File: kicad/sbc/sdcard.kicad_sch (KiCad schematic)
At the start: 12 parts, among them U14 7407, U15 SD_Card, U7 74125, U9 LP2950

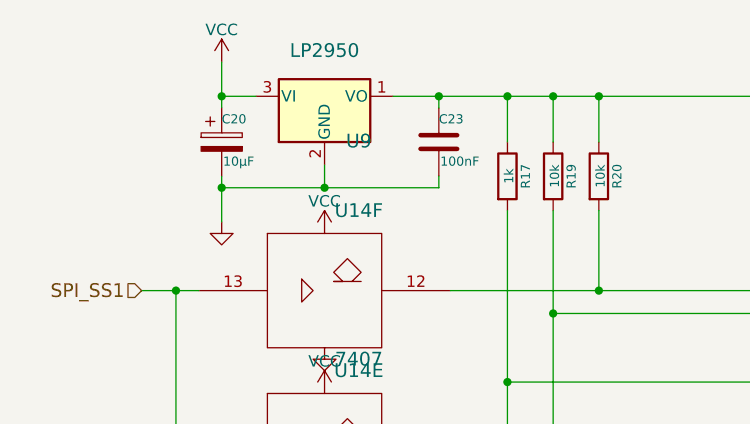
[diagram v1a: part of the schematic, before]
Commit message: cpld pinout
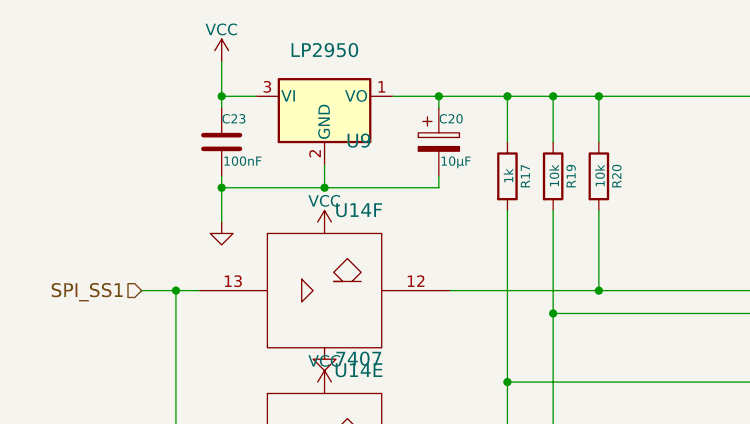
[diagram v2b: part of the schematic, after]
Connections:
- net VCC: now also C23.1; no longer C20.1
- net at C24.1, R17.1, R19.1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: now also C20.1; no longer C23.1
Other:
- moved on the sheet: C20, C23
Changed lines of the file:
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@@
     )
   )
-  (symbol (lib_id "Device:C_Polarized") (at 54.61 43.18 0) (unit 1)
-    (in_bom yes) (on_board yes) (dnp no)
-    (property "Reference" "C20" (at 54.61 40.64 0)
-      (effects (font (size 1.016 1.016)) (justify left))
-    )
-    (property "Value" "10µF" (at 54.7624 45.339 0)
-      (effects (font (size 1.016 1.016)) (justify left))
-    )
-    (property "Footprint" "Capacitor_THT:CP_Radial_D5.0mm_P2.50mm" (at 55.5752 46.99 0)
-      (effects (font (size 1.27 1.27)) hide)
-    )
-    (property "Datasheet" "~" (at 54.61 43.18 0)
+  (symbol (lib_id "Device:C_Polarized") (at 78.74 43.18 0) (unit 1)
+    (in_bom yes) (on_board yes) (dnp no)
+    (property "Reference" "C20" (at 78.74 40.64 0)
+      (effects (font (size 1.016 1.016)) (justify left))
+    )
+    (property "Value" "10µF" (at 78.8924 45.339 0)
+      (effects (font (size 1.016 1.016)) (justify left))
+    )
+    (property "Footprint" "Capacitor_THT:CP_Radial_D5.0mm_P2.50mm" (at 79.7052 46.99 0)
+      (effects (font (size 1.27 1.27)) hide)
+    )
+    (property "Datasheet" "~" (at 78.74 43.18 0)
       (effects (font (size 1.27 1.27)) hide)
     )
@@
     )
   )
-  (symbol (lib_id "Device:C") (at 78.74 43.18 0) (unit 1)
-    (in_bom yes) (on_board yes) (dnp no)
-    (property "Reference" "C23" (at 78.74 40.64 0)
-      (effects (font (size 1.016 1.016)) (justify left))
-    )
-    (property "Value" "100nF" (at 78.8924 45.339 0)
-      (effects (font (size 1.016 1.016)) (justify left))
-    )
-    (property "Footprint" "Capacitor_SMD:C_1206_3216Metric_Pad1.33x1.80mm_HandSolder" (at 79.7052 46.99 0)
-      (effects (font (size 1.27 1.27)) hide)
-    )
-    (property "Datasheet" "~" (at 78.74 43.18 0)
-      (effects (font (size 1.27 1.27)) hide)
-    )
+  (symbol (lib_id "Device:C") (at 54.61 43.18 0) (unit 1)
+    (in_bom yes) (on_board yes) (dnp no)
+    (property "Reference" "C23" (at 54.61 40.64 0)
+      (effects (font (size 1.016 1.016)) (justify left))
+    )
+    (property "Value" "100nF" (at 54.7624 45.339 0)
+      (effects (font (size 1.016 1.016)) (justify left))
+    )
+    (property "Footprint" "Capacitor_SMD:C_1206_3216Metric_Pad1.33x1.80mm_HandSolder" (at 55.5752 46.99 0)
+      (effects (font (size 1.27 1.27)) hide)
+    )
+    (property "Datasheet" "~" (at 54.61 43.18 0)
+      (effects (font (size 1.27 1.27)) hide)
+    )

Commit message: complete schematics
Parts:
- removed U15: SD_Card, Connector_Card:SD_TE_2041021, symbol Connector:SD_Card
- added U15: Micro_SD_Card_Det1, Connector_Card:microSD_HC_Hirose_DM3BT-DSF-PEJS, symbol Connector:Micro_SD_Card_Det1
- U14, U7: footprint Package_DIP:DIP-14_W7.62mm_Socket_LongPads -> Package_DIP:DIP-14_W7.62mm_LongPads
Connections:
- net GND: now also U15.10 (SHIELD), U15.4 (VDD)
- net SD_CARD_DETECT: now also U15.9 (DET)
- net at C20.1, C24.1, R17.1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: now also U15.6 (VSS)
- net DAT3: now reaches R20.2, U14.12
- net DAT3: now also U15.2 (DAT3/CD)
- net CMD: now reaches R19.2, U14.10
- net CMD: now also U15.3 (CMD)
- net CLK: now reaches R17.2, U14.8
- net CLK: now also U15.5 (CLK)
- net DAT0: now reaches U7.9 (D)
- net DAT0: now also U15.7 (DAT0)
- net DAT1: now reaches R21.2
- net DAT1: now also U15.8 (DAT1)
- net DAT2: now reaches R22.2
- net DAT2: now also U15.1 (DAT2)
- no-connect marks 2 -> 0

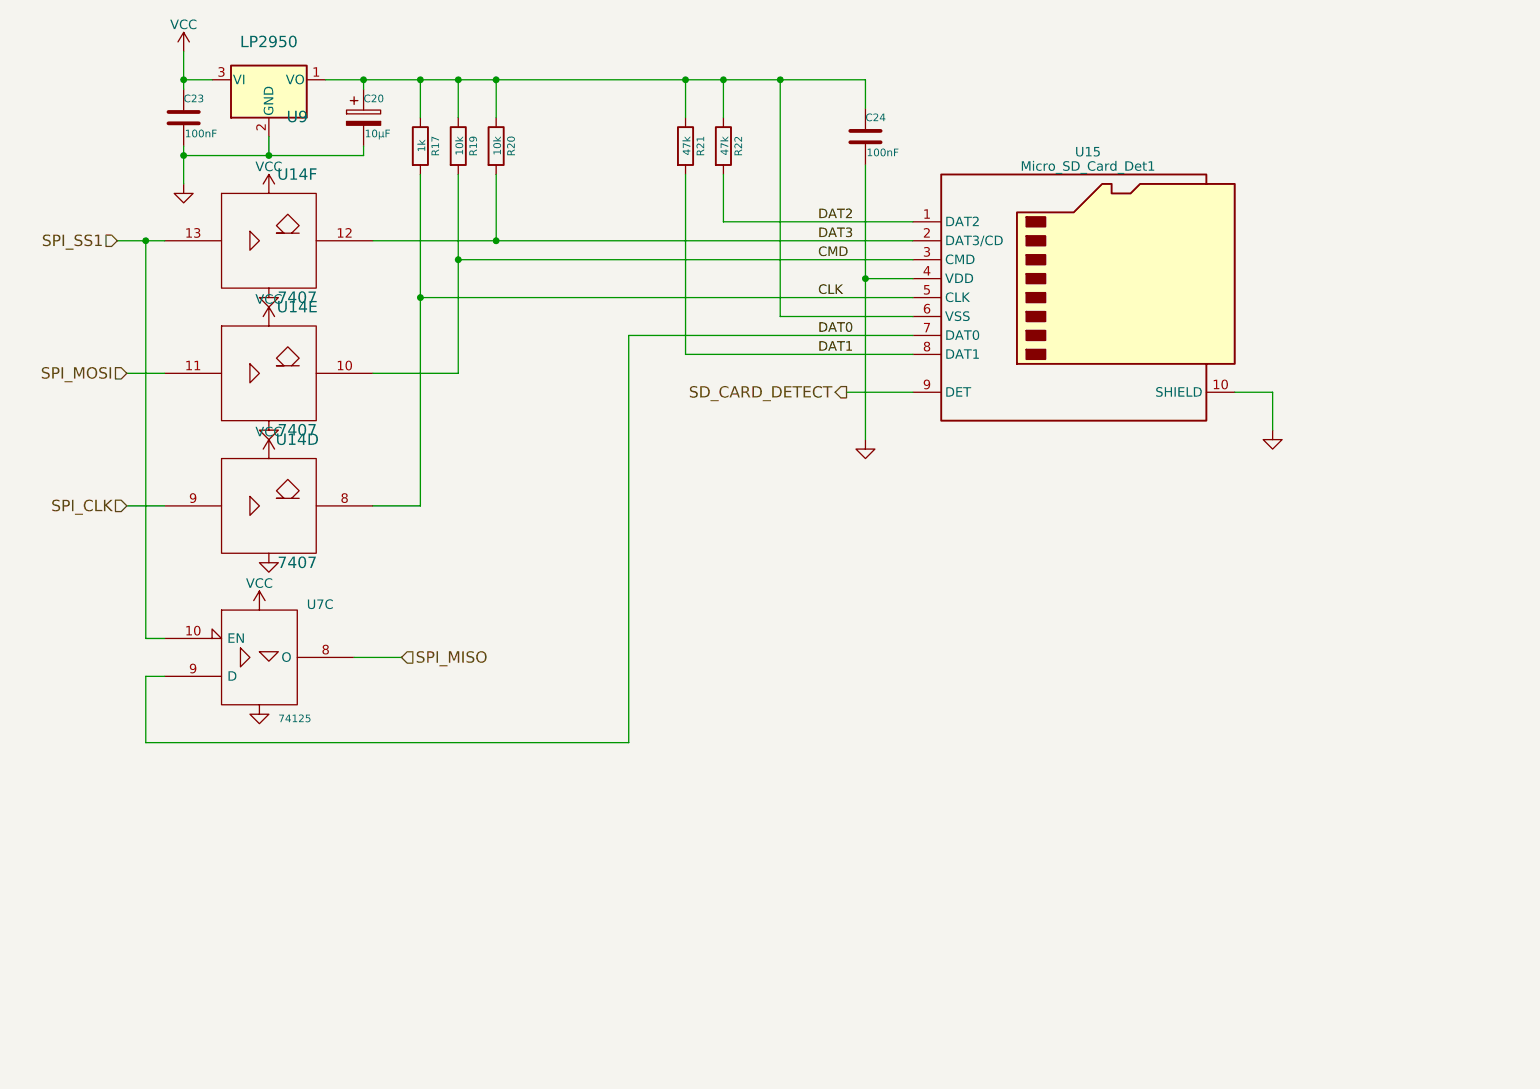
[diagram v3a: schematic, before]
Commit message: fix ERC messages
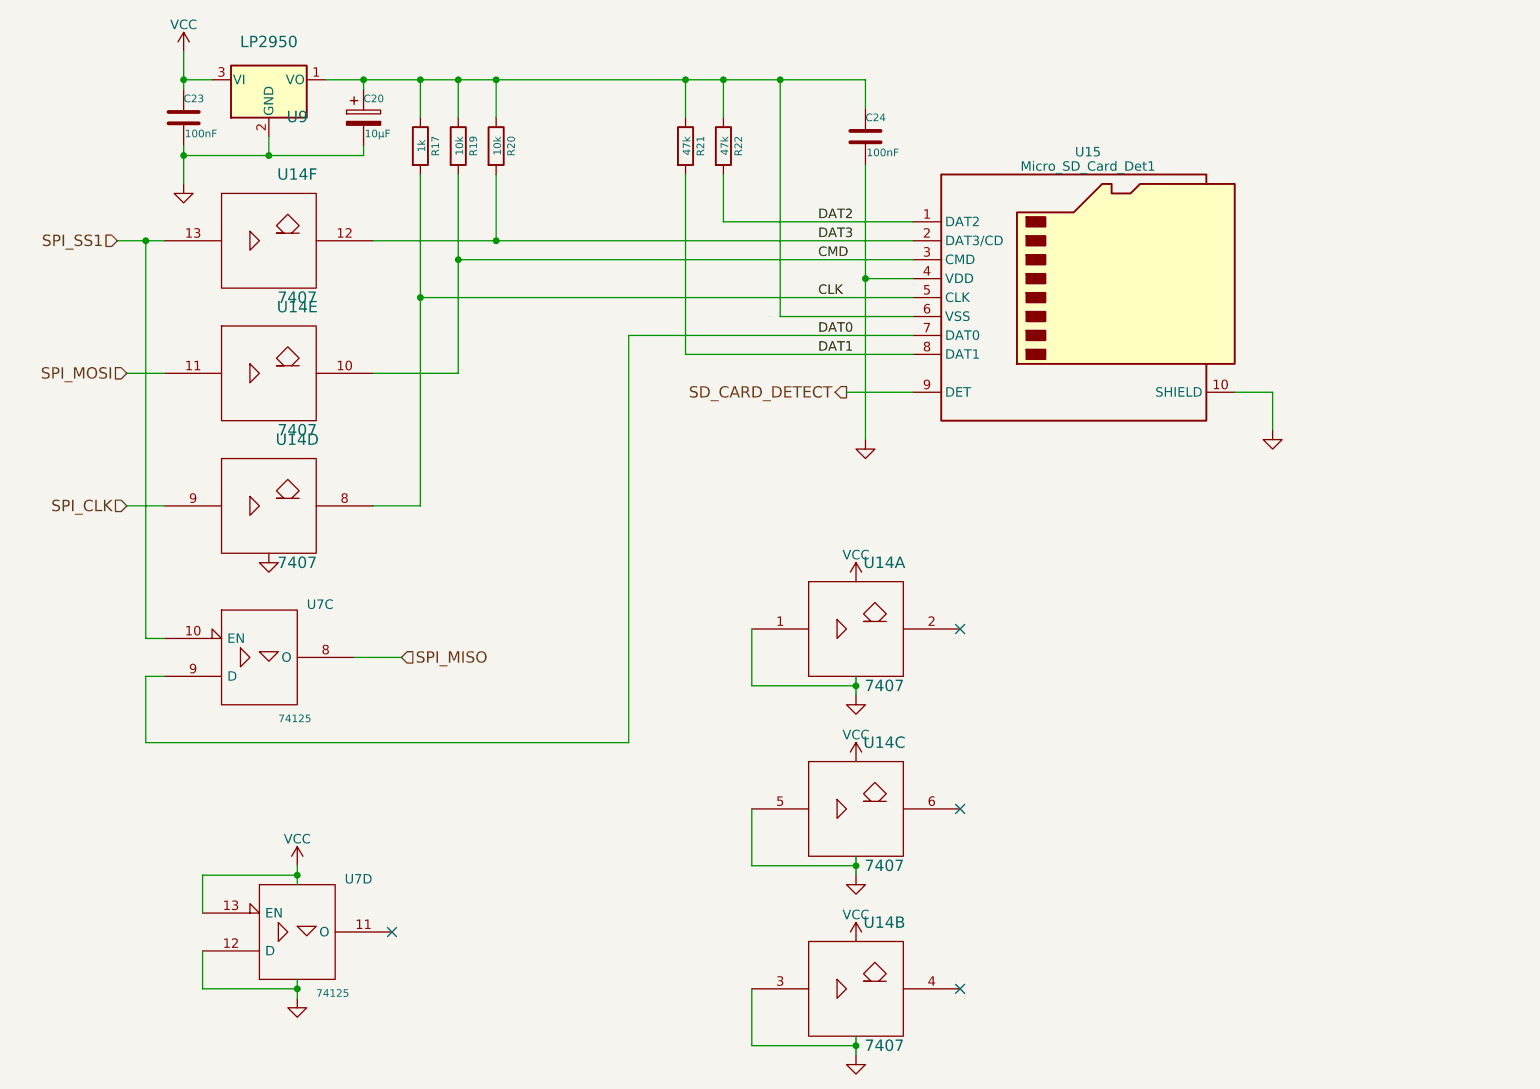
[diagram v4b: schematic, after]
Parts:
- added unit 1 of U14
- added unit 3 of U14
- added unit 2 of U14
- added unit 4 of U7
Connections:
- net GND: now also U14.1, U14.3, U14.5, U14.7 (Gnd), U14.7 (Gnd), U14.7 (Gnd), U7.12 (D), U7.7 (GND)
- net VCC: now also U14.14 (Vcc), U14.14 (Vcc), U14.14 (Vcc), U7.13 (EN), U7.14 (VCC)
- no-connect marks 0 -> 4

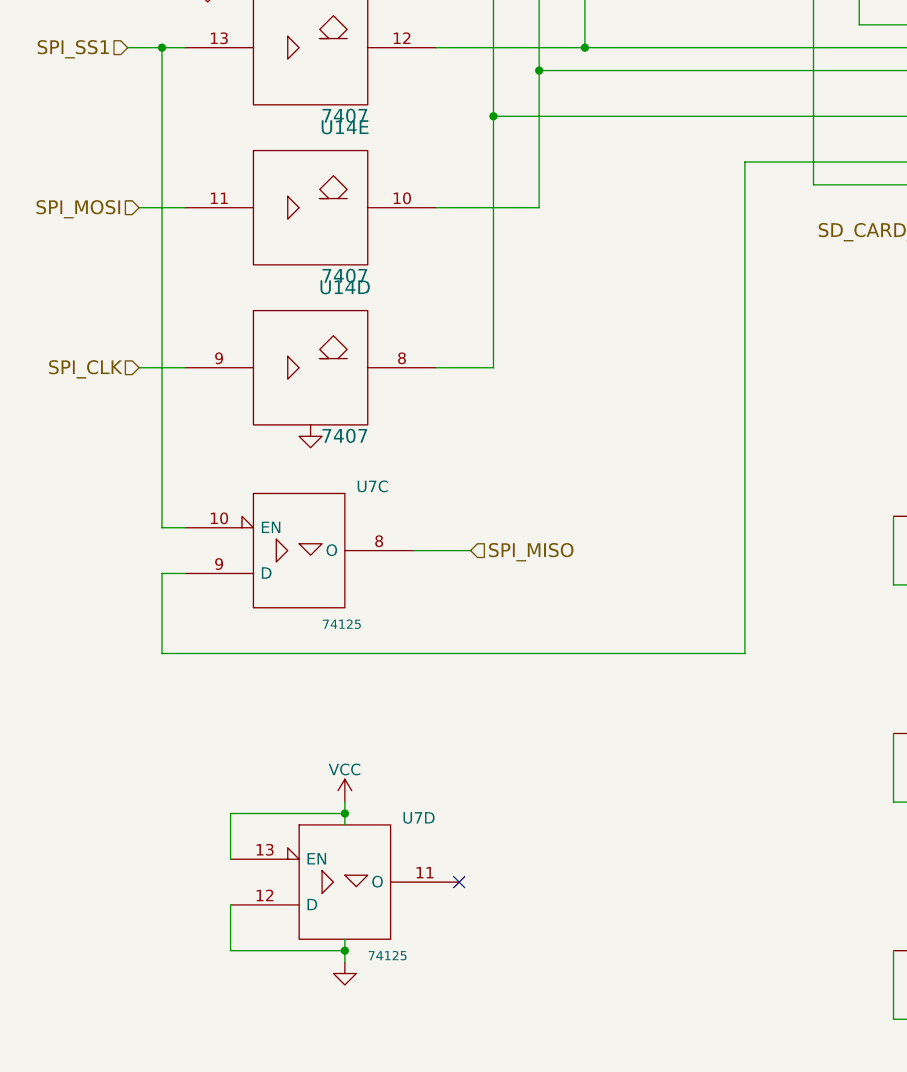
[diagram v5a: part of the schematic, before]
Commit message: erc cleanup
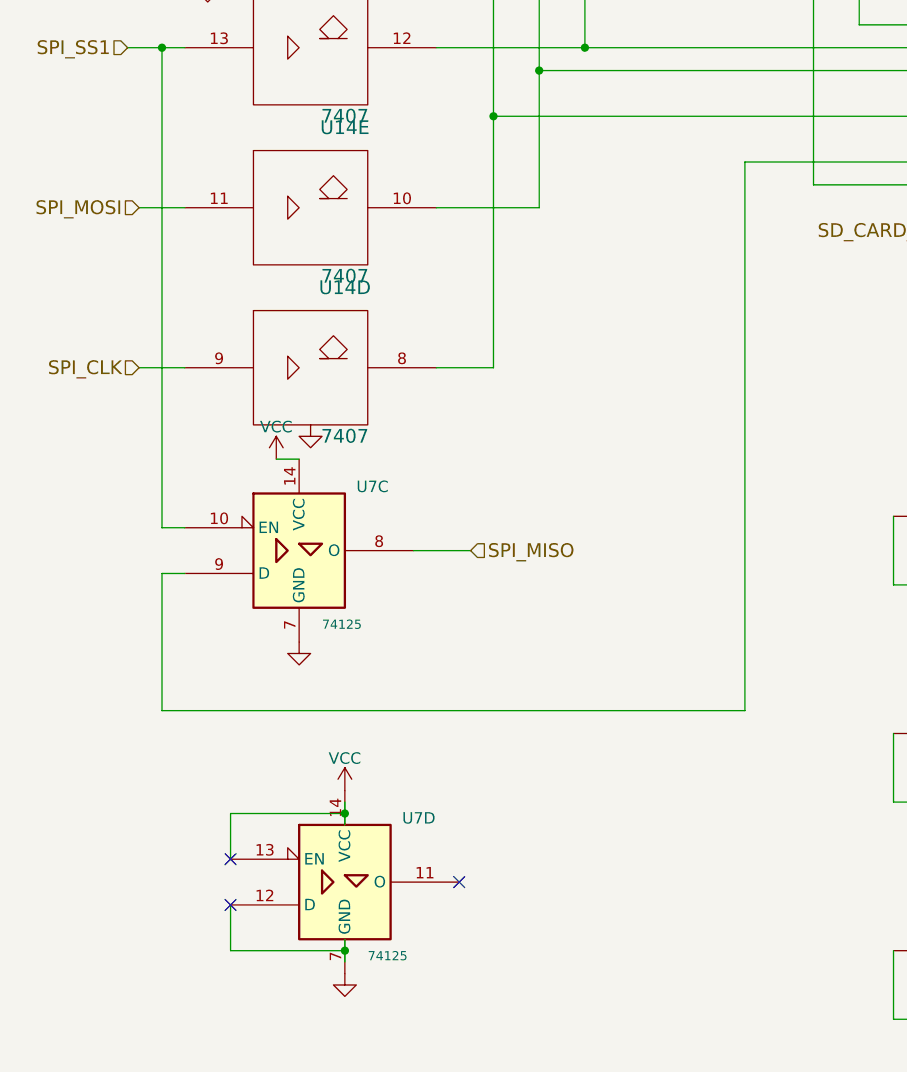
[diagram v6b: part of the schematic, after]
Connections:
- net GND: no longer U7.12 (D)
- net VCC: no longer U7.13 (EN)
- no-connect marks 4 -> 6

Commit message: regular sd socket separate masses for analog and digital cleanup routing
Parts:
- U15: footprint Connector_Card:microSD_HC_Hirose_DM3BT-DSF-PEJS -> Connector_Card:SD_Kyocera_145638009511859+
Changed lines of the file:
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@@
       (effects (font (size 1.27 1.27)))
     )
-    (property "Footprint" "Connector_Card:microSD_HC_Hirose_DM3BT-DSF-PEJS" (at 227.33 49.53 0)
+    (property "Footprint" "Connector_Card:SD_Kyocera_145638009511859+" (at 227.33 49.53 0)
       (effects (font (size 1.27 1.27)) hide)
     )
